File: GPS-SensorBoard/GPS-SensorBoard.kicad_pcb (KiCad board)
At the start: 2 copper layers, 50.8 x 25.4 mm, 19 parts, among them J1 ICSP, J2 POWER/CAN, J3 Conn_01x04, J4 Conn_01x04, U1 ATtiny841-SS, U2 MCP25625-x-SS, U3 74HC04

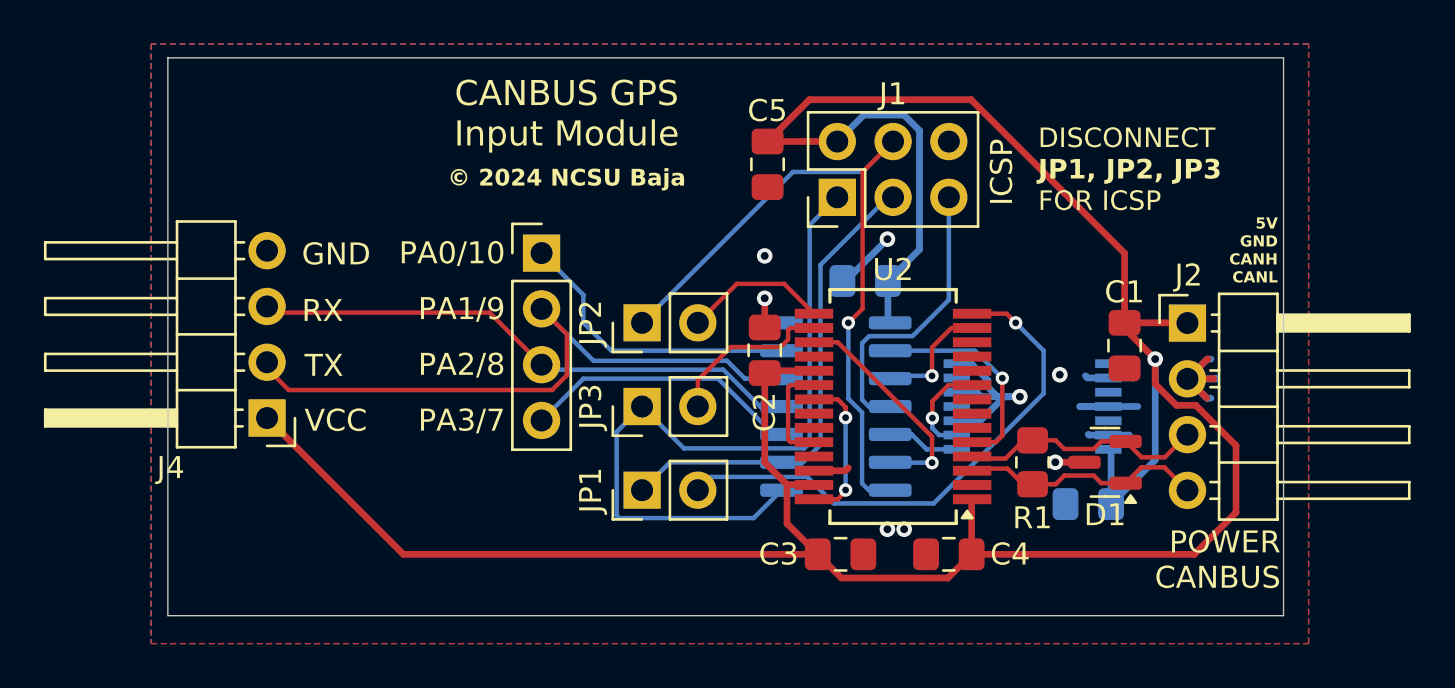
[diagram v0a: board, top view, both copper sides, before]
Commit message: Fixed grounds
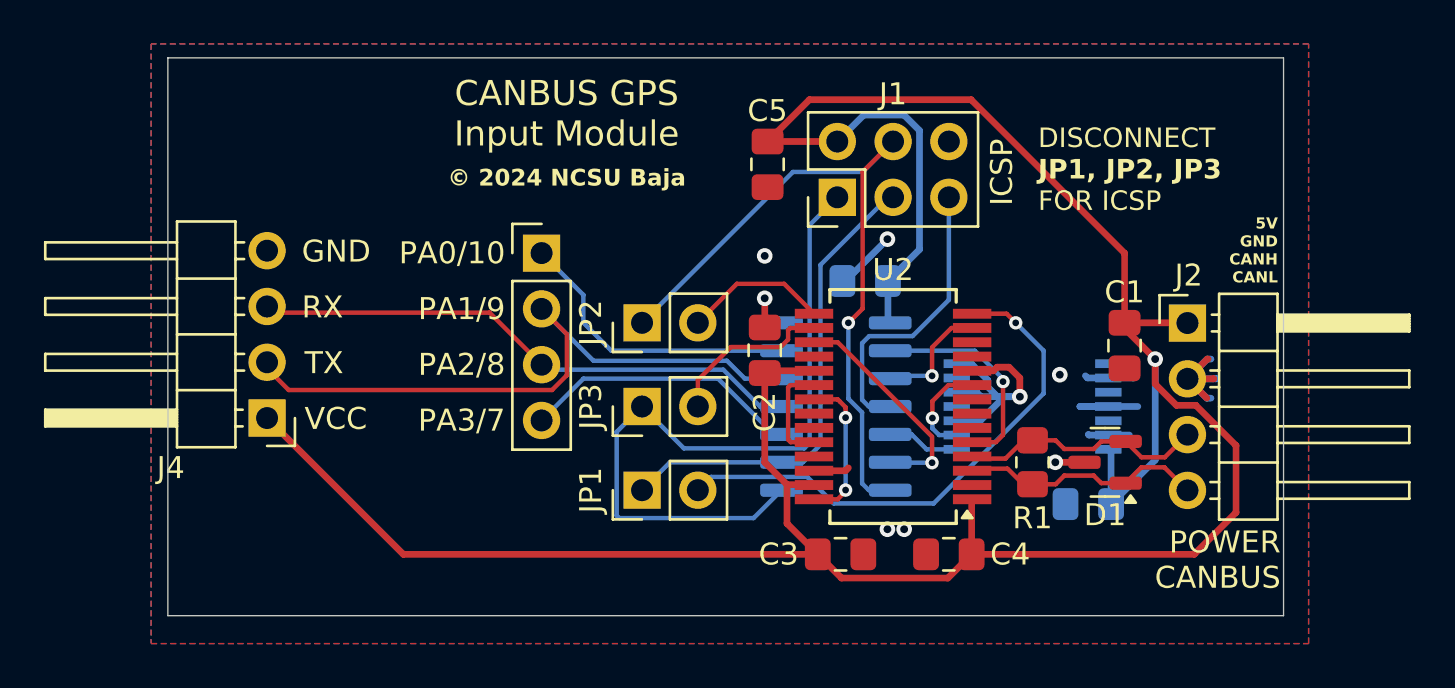
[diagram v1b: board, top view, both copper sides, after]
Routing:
- net GND: track 33.2 -> 36.5 mm
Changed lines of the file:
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@@
 		(tags "Through hole angled pin header THT 1x04 2.54mm single row")
 		(property "Reference" "J4"
-			(at 4.385 -2.27 360)
+			(at 4.385 -2.27 0)
 			(layer "F.SilkS")
 			(effects
@@
 		)
 		(property "Value" "Conn_01x04"
-			(at 4.385 9.89 360)
+			(at 4.385 9.89 0)
 			(layer "F.Fab")
 			(effects
@@
 	)
 	(gr_text "GND\n"
-		(at 116.078 98.425 0)
+		(at 116.078 98.298 0)
 		(layer "F.SilkS")
 		(effects
@@
 	)
 	(gr_text "VCC"
-		(at 116.205 106 0)
+		(at 116.205 105.918 0)
 		(layer "F.SilkS")
 		(effects
@@
 	)
 	(gr_text "TX\n"
-		(at 116.205 103.5 0)
+		(at 116.205 103.378 0)
 		(layer "F.SilkS")
 		(effects
@@
 	)
 	(gr_text "RX\n"
-		(at 116.078 101 0)
+		(at 116.078 100.838 0)
 		(layer "F.SilkS")
 		(effects
@@
 	)
 	(segment
+		(start 148.777826 103.475931)
+		(end 148.777826 104.327826)
+		(width 0.3048)
+		(layer "F.Cu")
+		(net 1)
+	)
+	(segment
+		(start 147.738141 102.98334)
+		(end 148.285235 102.98334)
+		(width 0.3048)
+		(layer "F.Cu")
+		(net 1)
+	)
+	(segment
 		(start 137.163 99.8504)
 		(end 137.16 99.8474)
@@
 	)
 	(segment
+		(start 148.285235 102.98334)
+		(end 148.777826 103.475931)
+		(width 0.3048)
+		(layer "F.Cu")
+		(net 1)
+	)
+	(segment
+		(start 147.571481 103.15)
+		(end 147.738141 102.98334)
+		(width 0.3048)
+		(layer "F.Cu")
+		(net 1)
+	)
+	(segment
 		(start 156.41 103.515)
 		(end 157.309 102.616)
@@
 	)
 	(segment
+		(start 146.605 103.15)
+		(end 147.571481 103.15)
+		(width 0.3048)
+		(layer "F.Cu")
+		(net 1)
+	)
+	(segment
 		(start 156.41 103.515)
 		(end 157.597 103.515)
@@
 	)
 	(segment
-		(start 147.979911 103.484701)
-		(end 147.979911 106.103289)
+		(start 147.6832 106.4)
+		(end 146.605 106.4)
 		(width 0.2032)
 		(layer "F.Cu")
@@
 	)
 	(segment
-		(start 147.6832 106.4)
-		(end 146.605 106.4)
+		(start 148.011688 103.64374)
+		(end 148.011688 106.071512)
 		(width 0.2032)
 		(layer "F.Cu")
@@
 	)
 	(segment
-		(start 147.979911 106.103289)
+		(start 148.011688 106.071512)
 		(end 147.6832 106.4)
 		(width 0.2032)
@@
 	)
 	(via
-		(at 147.979911 103.484701)
+		(at 148.011688 103.64374)
 		(size 0.6096)
 		(drill 0.3048)
@@
 	)
 	(segment
-		(start 147.979911 103.484701)
-		(end 147.974301 103.484701)
+		(start 146.7246 102.235)
+		(end 142.875 102.235)
 		(width 0.2032)
 		(layer "B.Cu")
@@
 	)
 	(segment
-		(start 146.7246 102.235)
-		(end 142.875 102.235)
+		(start 148.011688 103.522088)
+		(end 146.7246 102.235)
 		(width 0.2032)
 		(layer "B.Cu")
@@
 	)
 	(segment
-		(start 147.974301 103.484701)
-		(end 146.7246 102.235)
+		(start 148.011688 103.64374)
+		(end 148.011688 103.522088)
 		(width 0.2032)
 		(layer "B.Cu")

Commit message: GPS sensor board fix
Switched gnd and vcc
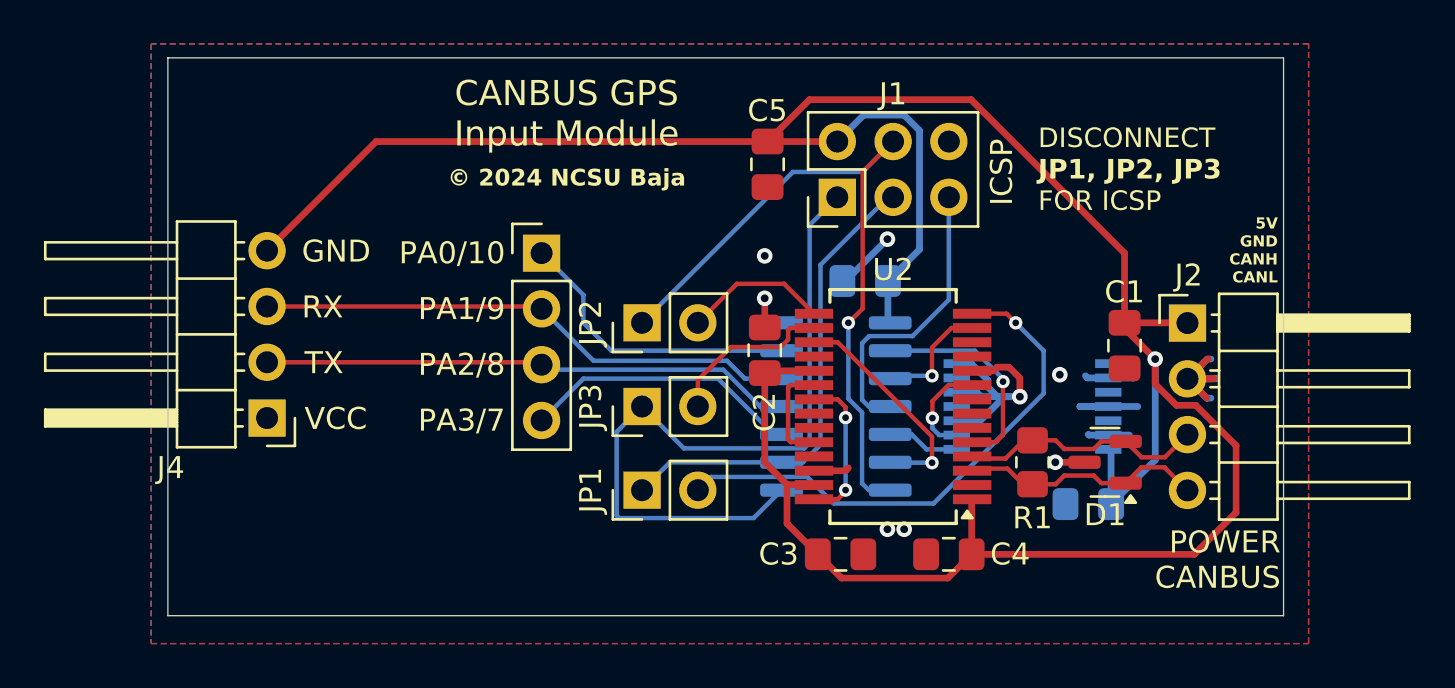
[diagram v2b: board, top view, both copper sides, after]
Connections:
- J4 pad 1: +5V -> GND
- J4 pad 2: /USER1 -> /USER2
- J4 pad 3: /USER2 -> /USER1
- J4 pad 4: GND -> +5V
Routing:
- net /USER1: track 30.1 -> 24.8 mm
- net +5V: track 128.0 -> 125.7 mm
- net /USER2: track 25.2 -> 24.3 mm
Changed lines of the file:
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@@
 		(property ki_fp_filters "Connector*:*_2x??_*")
 		(sheetname "Root")
-		(sheetfile "ATTINYSensorBoard.kicad_sch")
+		(sheetfile "GPS-SensorBoard.kicad_sch")
 		(attr through_hole)
 		(fp_line
@@
 		(property ki_fp_filters "C_*")
 		(sheetname "Root")
-		(sheetfile "ATTINYSensorBoard.kicad_sch")
+		(sheetfile "GPS-SensorBoard.kicad_sch")
 		(attr smd)
 		(fp_line
@@
 		(property ki_fp_filters "C_*")
 		(sheetname "Root")
-		(sheetfile "ATTINYSensorBoard.kicad_sch")
+		(sheetfile "GPS-SensorBoard.kicad_sch")
 		(attr smd)
 		(fp_line
@@
 		(property ki_fp_filters "Jumper* TestPoint*2Pads* TestPoint*Bridge*")
 		(sheetname "Root")
-		(sheetfile "ATTINYSensorBoard.kicad_sch")
+		(sheetfile "GPS-SensorBoard.kicad_sch")
 		(attr through_hole)
 		(fp_line
@@
 		(property ki_fp_filters "R_*")
 		(sheetname "Root")
-		(sheetfile "ATTINYSensorBoard.kicad_sch")
+		(sheetfile "GPS-SensorBoard.kicad_sch")
 		(attr smd)
 		(fp_line
@@
 		(property ki_fp_filters "Jumper* TestPoint*2Pads* TestPoint*Bridge*")
 		(sheetname "Root")
-		(sheetfile "ATTINYSensorBoard.kicad_sch")
+		(sheetfile "GPS-SensorBoard.kicad_sch")
 		(attr through_hole)
 		(fp_line
@@
 		(property ki_fp_filters "Connector*:*_1x??_*")
 		(sheetname "Root")
-		(sheetfile "ATTINYSensorBoard.kicad_sch")
+		(sheetfile "GPS-SensorBoard.kicad_sch")
 		(attr through_hole)
 		(fp_line
@@
 		(property ki_fp_filters "Connector*:*_1x??_*")
 		(sheetname "Root")
-		(sheetfile "ATTINYSensorBoard.kicad_sch")
+		(sheetfile "GPS-SensorBoard.kicad_sch")
 		(attr through_hole)
 		(fp_line
@@
 		)
 		(sheetname "Root")
-		(sheetfile "ATTINYSensorBoard.kicad_sch")
+		(sheetfile "GPS-SensorBoard.kicad_sch")
 		(attr smd)
 		(fp_line
@@
 		(property ki_fp_filters "Jumper* TestPoint*2Pads* TestPoint*Bridge*")
 		(sheetname "Root")
-		(sheetfile "ATTINYSensorBoard.kicad_sch")
+		(sheetfile "GPS-SensorBoard.kicad_sch")
 		(attr through_hole)
 		(fp_line
@@
 		(property ki_fp_filters "C_*")
 		(sheetname "Root")
-		(sheetfile "ATTINYSensorBoard.kicad_sch")
+		(sheetfile "GPS-SensorBoard.kicad_sch")
 		(attr smd)
 		(fp_line
@@
 		(property ki_fp_filters "Connector*:*_1x??_*")
 		(sheetname "Root")
-		(sheetfile "ATTINYSensorBoard.kicad_sch")
+		(sheetfile "GPS-SensorBoard.kicad_sch")
 		(attr through_hole)
 		(fp_line
@@
 			(layers "*.Cu" "*.Mask")
 			(remove_unused_layers no)
-			(net 2 "+5V")
+			(net 1 "GND")
 			(pinfunction "Pin_1")
 			(pintype "passive")
@@
 			(layers "*.Cu" "*.Mask")
 			(remove_unused_layers no)
-			(net 16 "/USER1")
+			(net 14 "/USER2")
 			(pinfunction "Pin_2")
 			(pintype "passive")
@@
 			(layers "*.Cu" "*.Mask")
 			(remove_unused_layers no)
-			(net 14 "/USER2")
+			(net 16 "/USER1")
 			(pinfunction "Pin_3")
 			(pintype "passive")
@@
 			(layers "*.Cu" "*.Mask")
 			(remove_unused_layers no)
-			(net 1 "GND")
+			(net 2 "+5V")
 			(pinfunction "Pin_4")
 			(pintype "passive")
@@
 		(property ki_fp_filters "C_*")
 		(sheetname "Root")
-		(sheetfile "ATTINYSensorBoard.kicad_sch")
+		(sheetfile "GPS-SensorBoard.kicad_sch")
 		(attr smd)
 		(fp_line
@@
 		(property ki_fp_filters "SSOP*5.3x10.2mm*P0.65mm*")
 		(sheetname "Root")
-		(sheetfile "ATTINYSensorBoard.kicad_sch")
+		(sheetfile "GPS-SensorBoard.kicad_sch")
 		(attr smd)
 		(fp_line
@@
 		(property ki_fp_filters "C_*")
 		(sheetname "Root")
-		(sheetfile "ATTINYSensorBoard.kicad_sch")
+		(sheetfile "GPS-SensorBoard.kicad_sch")
 		(attr smd)
 		(fp_line
@@
 		(property ki_fp_filters "SOIC*3.9x8.7mm*P1.27mm*")
 		(sheetname "Root")
-		(sheetfile "ATTINYSensorBoard.kicad_sch")
+		(sheetfile "GPS-SensorBoard.kicad_sch")
 		(attr smd)
 		(fp_line
@@
 		(property ki_fp_filters "DIP*W7.62mm* SSOP?14* TSSOP?14*")
 		(sheetname "Root")
-		(sheetfile "ATTINYSensorBoard.kicad_sch")
+		(sheetfile "GPS-SensorBoard.kicad_sch")
 		(attr smd)
 		(fp_line
@@
 		(property ki_fp_filters "C_*")
 		(sheetname "Root")
-		(sheetfile "ATTINYSensorBoard.kicad_sch")
+		(sheetfile "GPS-SensorBoard.kicad_sch")
 		(attr smd)
 		(fp_line
@@
 		(property ki_fp_filters "C_*")
 		(sheetname "Root")
-		(sheetfile "ATTINYSensorBoard.kicad_sch")
+		(sheetfile "GPS-SensorBoard.kicad_sch")
 		(attr smd)
 		(fp_line
@@
 	)
 	(segment
+		(start 114.5 97.68)
+		(end 119.47 92.71)
+		(width 0.3048)
+		(layer "F.Cu")
+		(net 2)
+	)
+	(segment
 		(start 139.195 90.805)
 		(end 137.29 92.71)
@@
 	)
 	(segment
-		(start 138.176 108.331)
-		(end 137.163 107.318)
+		(start 114.063 97.68)
+		(end 114.5 97.68)
 		(width 0.3048)
 		(layer "F.Cu")
@@
 	)
 	(segment
-		(start 120.706 111.506)
-		(end 139.576 111.506)
+		(start 138.176 108.331)
+		(end 137.163 107.318)
 		(width 0.3048)
 		(layer "F.Cu")
@@
 	)
 	(segment
-		(start 114.5 105.3)
-		(end 120.706 111.506)
-		(width 0.3048)
-		(layer "F.Cu")
-		(net 2)
-	)
-	(segment
 		(start 153.546 101.222)
 		(end 154.94 102.616)
@@
 	)
 	(segment
+		(start 114.063 97.68)
+		(end 114.046 97.663)
+		(width 0.3048)
+		(layer "F.Cu")
+		(net 2)
+	)
+	(segment
 		(start 156.718 111.506)
 		(end 158.623 109.601)
@@
 		(net 2)
 	)
+	(segment
+		(start 119.47 92.71)
+		(end 137.29 92.71)
+		(width 0.3048)
+		(layer "F.Cu")
+		(net 2)
+	)
 	(via
 		(at 154.94 102.616)
@@
 	)
 	(segment
-		(start 114.5 100.5)
-		(end 124.63 100.5)
+		(start 114.5 102.76)
+		(end 126.89 102.76)
 		(width 0.2032)
 		(layer "F.Cu")
@@
 	)
 	(segment
-		(start 124.63 100.5)
+		(start 126.89 102.76)
 		(end 127 102.87)
 		(width 0.2032)
@@
 	)
 	(segment
-		(start 128.1548 101.4848)
-		(end 128.1548 103.348334)
-		(width 0.2032)
-		(layer "F.Cu")
-		(net 16)
-	)
-	(segment
-		(start 128.1548 103.348334)
-		(end 127.478334 104.0248)
-		(width 0.2032)
-		(layer "F.Cu")
-		(net 16)
-	)
-	(segment
-		(start 115.4848 104.0248)
-		(end 114.5 103.04)
-		(width 0.2032)
-		(layer "F.Cu")
-		(net 16)
-	)
-	(segment
-		(start 127.478334 104.0248)
-		(end 115.4848 104.0248)
+		(start 126.89 100.22)
+		(end 127 100.33)
 		(width 0.2032)
 		(layer "F.Cu")
@@
 	)
 	(segment
-		(start 127 100.33)
-		(end 128.1548 101.4848)
+		(start 114.5 100.22)
+		(end 126.89 100.22)
 		(width 0.2032)
 		(layer "F.Cu")
